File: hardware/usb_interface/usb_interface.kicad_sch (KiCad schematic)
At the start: 26 parts, among them P1 USB_C_Plug_USB2.0, Q1 2N7002, Q3 IRLML6401, Q4 IRLML6401, U1 MAX14689, U2 AD8541, U3 AD8541, U4 AD8541

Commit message: lv backup hw update, usb interface hw update, MCU pinout spreadsheet
added spreadsheet for mapping / allocating MCU pins and resources

updated LV backup schematic with divider / buffer amplifier for MCU measurement

updated USB interface voltage buffers: all have high-impedance /2 buffers
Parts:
- added R12, R13, R14, R15: 1Meg, Resistor_SMD:R_0402_1005Metric_Pad0.72x0.64mm_HandSolder, symbol Device:R_US
- R5, R8: value 100k -> 1Meg
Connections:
- net BUS: now also R14.1; no longer R8.1
- net CC1: now also R12.1; no longer U2.3 (+)
- net CC2: now also R8.1; no longer U3.3 (+)
- net GND: now also R13.2, R15.2
- net VBUS/2 renamed V_{BUS}
- new net: R12.2, R5.1, U2.3 (+)
- new net: R14.2, R15.1, U4.3 (+)
- new net: R13.1, R8.2, U3.3 (+)
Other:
- moved on the sheet: C3, U2

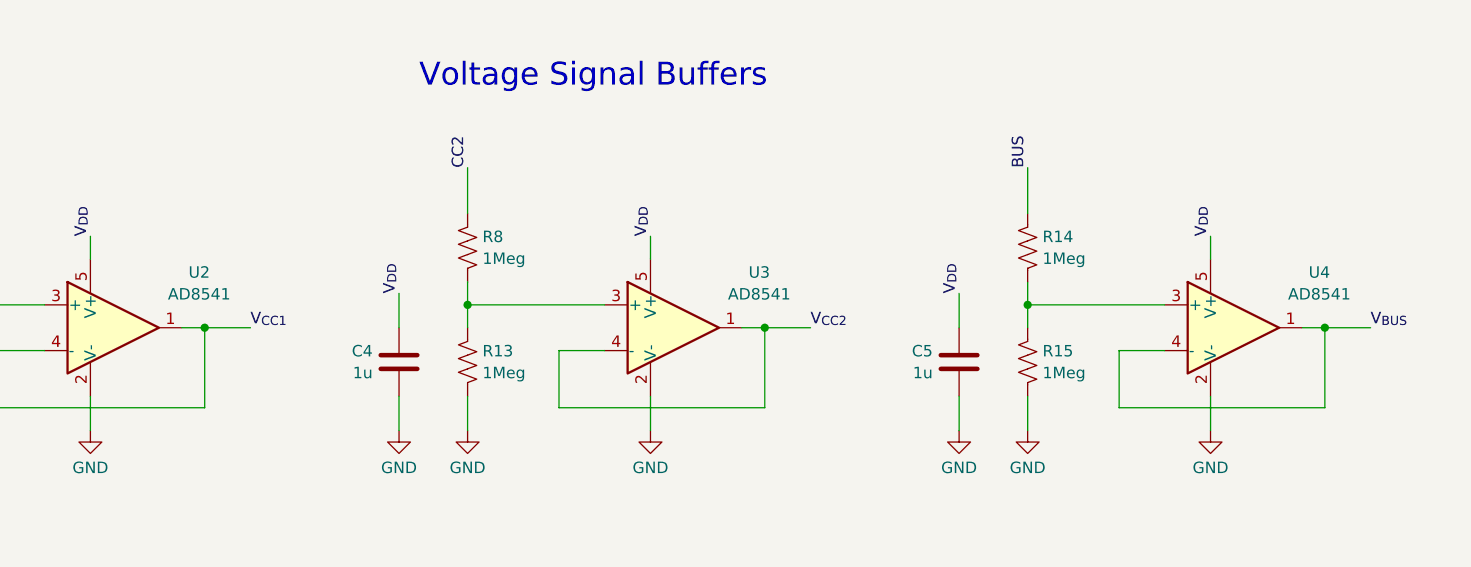
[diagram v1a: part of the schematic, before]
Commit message: hw amplifier change in lv backup and usb interface
replaced AD8541 operational amplifier with MCP6006 (massive cost savings, on order of $1 per chip or more)
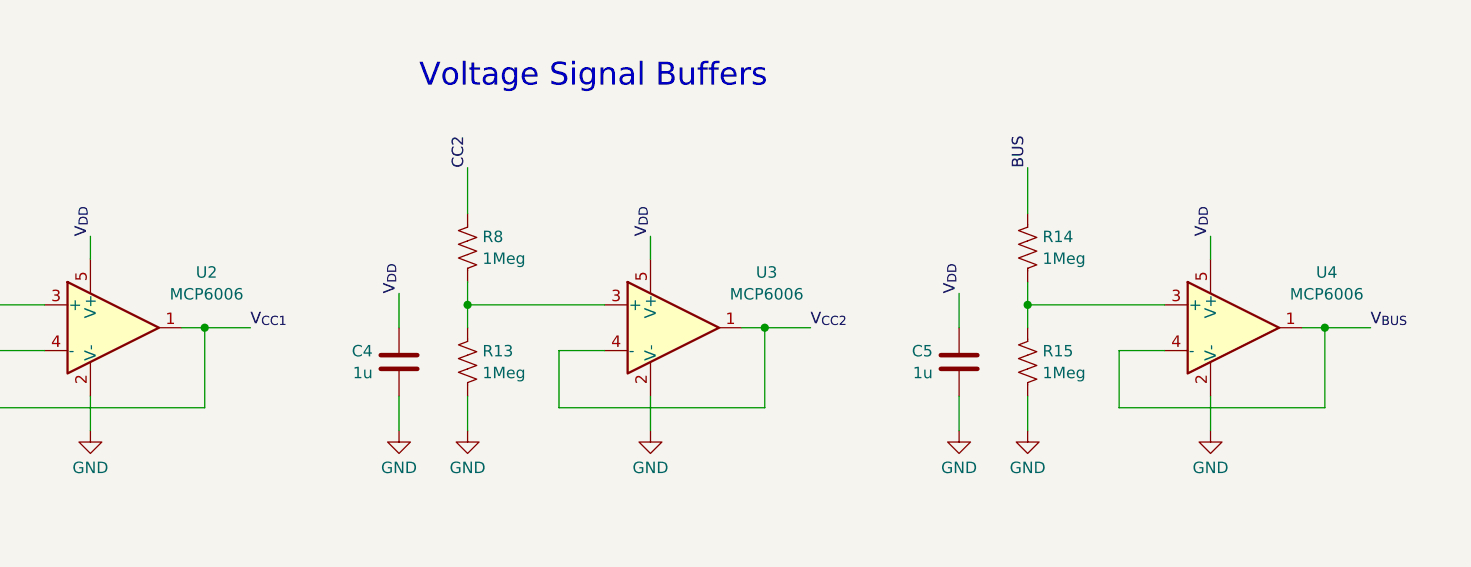
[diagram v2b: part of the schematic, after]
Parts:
- removed U2, U3, U4: AD8541, Package_TO_SOT_SMD:TSOT-23-5, symbol HPB_symbols:AD8541
- added U2, U3, U4: MCP6006, Package_TO_SOT_SMD:TSOT-23-5, symbol HPB_symbols:MCP6006
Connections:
- net GND: now also U2.2 (V-), U3.2 (V-), U4.2 (V-)
- net PWR: now also U2.5 (V+), U3.5 (V+), U4.5 (V+)
- net V_{BUS}: now also U4.1, U4.4 (-)
- net V_{CC1}: now also U2.1, U2.4 (-)
- net V_{CC2}: now also U3.1, U3.4 (-)
- net at R12.2, R5.1: now also U2.3 (+)
- net at R14.2, R15.1: now also U4.3 (+)
- net at R13.1, R8.2: now also U3.3 (+)
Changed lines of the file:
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@@
+	)
+	(symbol
+		(lib_id "HPB_symbols:MCP6006")
+		(at 132.08 138.43 0)
+		(unit 1)
+		(exclude_from_sim no)
+		(in_bom yes)
+		(on_board yes)
+		(dnp no)
+		(fields_autoplaced yes)
+		(property "Reference" "U2"
+			(at 142.4479 132.285 0)
+			(effects
+				(font
+					(size 1.27 1.27)
+				)
+			)
+		)
+		(property "Value" "MCP6006"
+			(at 142.4479 134.7093 0)
+			(effects
+				(font
+					(size 1.27 1.27)
+				)
+			)
+		)
+		(property "Footprint" "Package_TO_SOT_SMD:TSOT-23-5"
+			(at 132.08 138.43 0)
+			(effects
+				(font
+					(size 1.27 1.27)
+				)
+				(hide yes)
+			)
+		)
+		(property "Datasheet" "https://ww1.microchip.com/downloads/aemDocuments/documents/APID/ProductDocuments/DataSheets/MCP6006-6R-6U-7-9-Data-Sheet-20006411B.pdf"
+			(at 132.08 133.35 0)
+			(effects
+				(font
+					(size 1.27 1.27)
+				)
+				(hide yes)
+			)
+		)
+		(property "Description" "Amplifier, Operational, 1MHz, 5V, TSOT-23-5"
+			(at 132.08 138.43 0)
+			(effects
+				(font
+					(size 1.27 1.27)
+				)
+				(hide yes)
+			)
+		)
+		(pin "4"
+		)
+		(pin "1"
+		)
+		(pin "3"
+		)
+		(pin "2"
+		)
+		(pin "5"
+		)
+		(instances
+			(project ""
+				(path "/2e1f00c8-9310-48e9-8715-c5b76c2b7c3f"
+					(reference "U2")
+					(unit 1)
+				)
+			)
+		)
 	)
 	(symbol
@@
 	)
 	(symbol
-		(lib_id "HPB_symbols:AD8541")
-		(at 256.54 138.43 0)
-		(unit 1)
-		(exclude_from_sim no)
-		(in_bom yes)
-		(on_board yes)
-		(dnp no)
-		(fields_autoplaced yes)
-		(property "Reference" "U4"
-			(at 266.0915 132.285 0)
-			(effects
-				(font
-					(size 1.27 1.27)
-				)
-			)
-		)
-		(property "Value" "AD8541"
-			(at 266.0915 134.7093 0)
-			(effects
-				(font
-					(size 1.27 1.27)
-				)
-			)
-		)
-		(property "Footprint" "Package_TO_SOT_SMD:TSOT-23-5"
-			(at 256.54 138.43 0)
-			(effects
-				(font
-					(size 1.27 1.27)
-				)
-				(hide yes)
-			)
-		)
-		(property "Datasheet" "https://www.analog.com/media/en/technical-documentation/data-sheets/ad8541_8542_8544.pdf"
-			(at 256.54 133.35 0)
-			(effects
-				(font
-					(size 1.27 1.27)
-				)
-				(hide yes)
-			)
-		)
-		(property "Description" "Precision Micropower, Low Noise CMOS, Rail-to-Rail Input/Output Operational Amplifier, TSOT-23-5"
-			(at 256.54 138.43 0)
-			(effects
-				(font
-					(size 1.27 1.27)
-				)
-				(hide yes)
-			)
-		)
-		(pin "2"
-		)
-		(pin "4"
-		)
-		(pin "1"
-		)
-		(pin "3"
-		)
-		(pin "5"
-		)
-		(instances
-			(project "usb_interface"
-				(path "/2e1f00c8-9310-48e9-8715-c5b76c2b7c3f"
-					(reference "U4")
-					(unit 1)
-				)
-			)
-		)
-	)
-	(symbol
 		(lib_id "HPB_symbols:MAX14689AETB")
 		(at 143.51 64.77 0)
@@
 	)
 	(symbol
+		(lib_id "HPB_symbols:MCP6006")
+		(at 194.31 138.43 0)
+		(unit 1)
+		(exclude_from_sim no)
+		(in_bom yes)
+		(on_board yes)
+		(dnp no)
+		(fields_autoplaced yes)
+		(property "Reference" "U3"
+			(at 204.6779 132.285 0)
+			(effects
+				(font
+					(size 1.27 1.27)
+				)
+			)
+		)
+		(property "Value" "MCP6006"
+			(at 204.6779 134.7093 0)
+			(effects
+				(font
+					(size 1.27 1.27)
+				)
+			)
+		)
+		(property "Footprint" "Package_TO_SOT_SMD:TSOT-23-5"
+			(at 194.31 138.43 0)
+			(effects
+				(font
+					(size 1.27 1.27)
+				)
+				(hide yes)
+			)
+		)
+		(property "Datasheet" "https://ww1.microchip.com/downloads/aemDocuments/documents/APID/ProductDocuments/DataSheets/MCP6006-6R-6U-7-9-Data-Sheet-20006411B.pdf"
+			(at 194.31 133.35 0)
+			(effects
+				(font
+					(size 1.27 1.27)
+				)
+				(hide yes)
+			)
+		)
+		(property "Description" "Amplifier, Operational, 1MHz, 5V, TSOT-23-5"
+			(at 194.31 138.43 0)
+			(effects
+				(font
+					(size 1.27 1.27)
+				)
+				(hide yes)
+			)
+		)
+		(pin "4"
+		)
+		(pin "1"
+		)
+		(pin "3"
+		)
+		(pin "2"
+		)
+		(pin "5"
+		)
+		(instances
+			(project "usb_interface"
+				(path "/2e1f00c8-9310-48e9-8715-c5b76c2b7c3f"
+					(reference "U3")
+					(unit 1)
+				)
+			)
+		)
+	)
+	(symbol
 		(lib_id "Device:R_US")
 		(at 171.45 129.54 0)
@@
 	)
 	(symbol
+		(lib_id "HPB_symbols:MCP6006")
+		(at 256.54 138.43 0)
+		(unit 1)
+		(exclude_from_sim no)
+		(in_bom yes)
+		(on_board yes)
+		(dnp no)
+		(fields_autoplaced yes)
+		(property "Reference" "U4"
+			(at 266.9079 132.285 0)
+			(effects
+				(font
+					(size 1.27 1.27)
+				)
+			)
+		)
+		(property "Value" "MCP6006"
+			(at 266.9079 134.7093 0)
+			(effects
+				(font
+					(size 1.27 1.27)
+				)
+			)
+		)
+		(property "Footprint" "Package_TO_SOT_SMD:TSOT-23-5"
+			(at 256.54 138.43 0)
+			(effects
+				(font
+					(size 1.27 1.27)
+				)
+				(hide yes)
+			)
+		)
+		(property "Datasheet" "https://ww1.microchip.com/downloads/aemDocuments/documents/APID/ProductDocuments/DataSheets/MCP6006-6R-6U-7-9-Data-Sheet-20006411B.pdf"
+			(at 256.54 133.35 0)
+			(effects
+				(font
+					(size 1.27 1.27)
+				)
+				(hide yes)
+			)
+		)
+		(property "Description" "Amplifier, Operational, 1MHz, 5V, TSOT-23-5"
+			(at 256.54 138.43 0)
+			(effects
+				(font
+					(size 1.27 1.27)
+				)
+				(hide yes)
+			)
+		)
+		(pin "4"
+		)
+		(pin "1"
+		)
+		(pin "3"
+		)
+		(pin "2"
+		)
+		(pin "5"
+		)
+		(instances
+			(project "usb_interface"
+				(path "/2e1f00c8-9310-48e9-8715-c5b76c2b7c3f"
+					(reference "U4")
+					(unit 1)
+				)
+			)
+		)
+	)
+	(symbol
 		(lib_id "Device:R_US")
 		(at 233.68 129.54 0)
@@
 	)
 	(symbol
-		(lib_id "HPB_symbols:AD8541")
-		(at 194.31 138.43 0)
-		(unit 1)
-		(exclude_from_sim no)
-		(in_bom yes)
-		(on_board yes)
-		(dnp no)
-		(fields_autoplaced yes)
-		(property "Reference" "U3"
-			(at 203.8615 132.285 0)
-			(effects
-				(font
-					(size 1.27 1.27)
-				)
-			)
-		)
-		(property "Value" "AD8541"
-			(at 203.8615 134.7093 0)
-			(effects
-				(font
-					(size 1.27 1.27)
-				)
-			)
-		)
-		(property "Footprint" "Package_TO_SOT_SMD:TSOT-23-5"
-			(at 194.31 138.43 0)
-			(effects
-				(font
-					(size 1.27 1.27)
-				)
-				(hide yes)
-			)
-		)
-		(property "Datasheet" "https://www.analog.com/media/en/technical-documentation/data-sheets/ad8541_8542_8544.pdf"
-			(at 194.31 133.35 0)
-			(effects
-				(font
-					(size 1.27 1.27)
-				)
-				(hide yes)
-			)
-		)
-		(property "Description" "Precision Micropower, Low Noise CMOS, Rail-to-Rail Input/Output Operational Amplifier, TSOT-23-5"
-			(at 194.31 138.43 0)
-			(effects
-				(font
-					(size 1.27 1.27)
-				)
-				(hide yes)
-			)
-		)
-		(pin "2"
-		)
-		(pin "4"
-		)
-		(pin "1"
-		)
-		(pin "3"
-		)
-		(pin "5"
-		)
-		(instances
-			(project "usb_interface"
-				(path "/2e1f00c8-9310-48e9-8715-c5b76c2b7c3f"
-					(reference "U3")
-					(unit 1)
-				)
-			)
-		)
-	)
-	(symbol
 		(lib_id "Device:R_US")
 		(at 43.18 153.67 0)
@@
 					(unit 1)
 				)
-			)
-		)
-	)
-	(symbol
-		(lib_id "HPB_symbols:AD8541")
-		(at 132.08 138.43 0)
-		(unit 1)
-		(exclude_from_sim no)
-		(in_bom yes)
-		(on_board yes)
-		(dnp no)
-		(fields_autoplaced yes)
-		(property "Reference" "U2"
-			(at 141.6315 132.285 0)
-			(effects
-				(font
-					(size 1.27 1.27)
-				)
-			)
-		)
-		(property "Value" "AD8541"
-			(at 141.6315 134.7093 0)
-			(effects
-				(font
-					(size 1.27 1.27)
-				)
-			)
-		)
-		(property "Footprint" "Package_TO_SOT_SMD:TSOT-23-5"
-			(at 132.08 138.43 0)
-			(effects
-				(font
-					(size 1.27 1.27)
-				)
-				(hide yes)
-			)
-		)
-		(property "Datasheet" "https://www.analog.com/media/en/technical-documentation/data-sheets/ad8541_8542_8544.pdf"
-			(at 132.08 133.35 0)
-			(effects
-				(font
-					(size 1.27 1.27)
-				)
-				(hide yes)
-			)
-		)
-		(property "Description" "Precision Micropower, Low Noise CMOS, Rail-to-Rail Input/Output Operational Amplifier, TSOT-23-5"
-			(at 132.08 138.43 0)
-			(effects
-				(font
-					(size 1.27 1.27)
-				)
-				(hide yes)
-			)
-		)
-		(pin "2"
-		)
-		(pin "4"
-		)
-		(pin "1"
-		)
-		(pin "3"
-		)
-		(pin "5"
-		)
-		(instances
-			(project ""
-				(path "/2e1f00c8-9310-48e9-8715-c5b76c2b7c3f"
-					(reference "U2")
-					(unit 1)
-				)
